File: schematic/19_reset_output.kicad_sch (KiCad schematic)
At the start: 11 parts, among them U403 74HC14, U420 74HC14, U424 74HC32, U425 74HC08, U705 TMUX6219DGKR

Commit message: pick controls and start pcb placement
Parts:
- U705: footprint Package_SO:VSSOP-8_3x3mm_P0.65mm -> Arpeggiator:VSSOP-8_DGK0008A_TI
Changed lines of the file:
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@@
       )
     )
-    (property "Footprint" "Package_SO:VSSOP-8_3x3mm_P0.65mm"
+    (property "Footprint" "Arpeggiator:VSSOP-8_DGK0008A_TI"
       (at 82.55 160.01999999999998 0.0)
       (effects

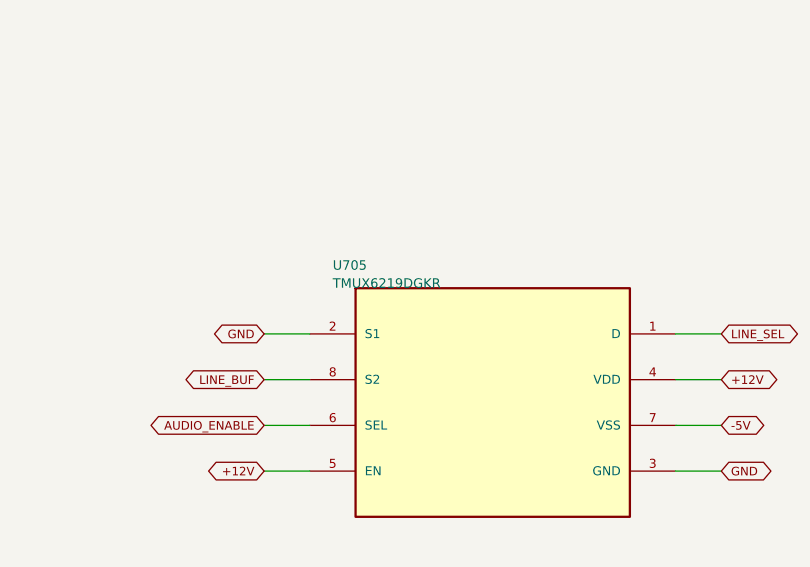
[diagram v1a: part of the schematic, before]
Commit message: parts and cheaper PCB files
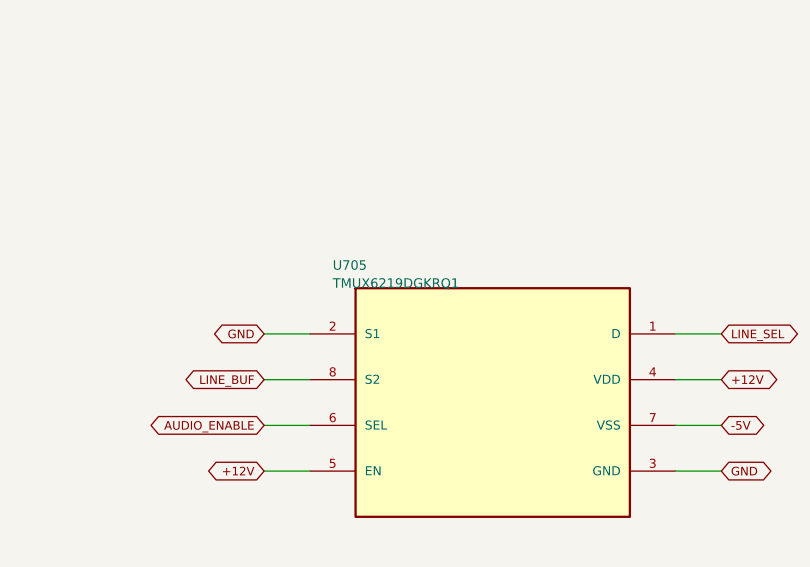
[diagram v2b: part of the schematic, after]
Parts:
- U705: value TMUX6219DGKR -> TMUX6219DGKRQ1; MPN TMUX6219DGKR -> TMUX6219DGKRQ1
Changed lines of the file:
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@@
       )
     )
-    (property "Value" "TMUX6219DGKR"
+    (property "Value" "TMUX6219DGKRQ1"
       (at 82.55 162.01999999999998 0.0)
       (effects
@@
       )
     )
-    (property "Datasheet" "https://www.ti.com/lit/ds/symlink/tmux6219.pdf"
+    (property "Datasheet" "https://www.ti.com/lit/ds/symlink/tmux6219-q1.pdf"
       (at 82.55 160.01999999999998 0.0)
       (effects
@@
       )
     )
-    (property "MPN" "TMUX6219DGKR"
+    (property "MPN" "TMUX6219DGKRQ1"
       (at 100.33 175.26 0.0)
       (effects
